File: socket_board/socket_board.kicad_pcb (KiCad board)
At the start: 2 copper layers, 90.2 x 35.6 mm, 8 parts, among them J1 Barrel_Jack_Switch, J2 DIN-5_180degree, J3 DIN-5_180degree, J4 AudioJack3, J5 AudioJack3, J6 Conn_01x02_Male, J7 Conn_01x04_Male, J8 Conn_01x05_Male

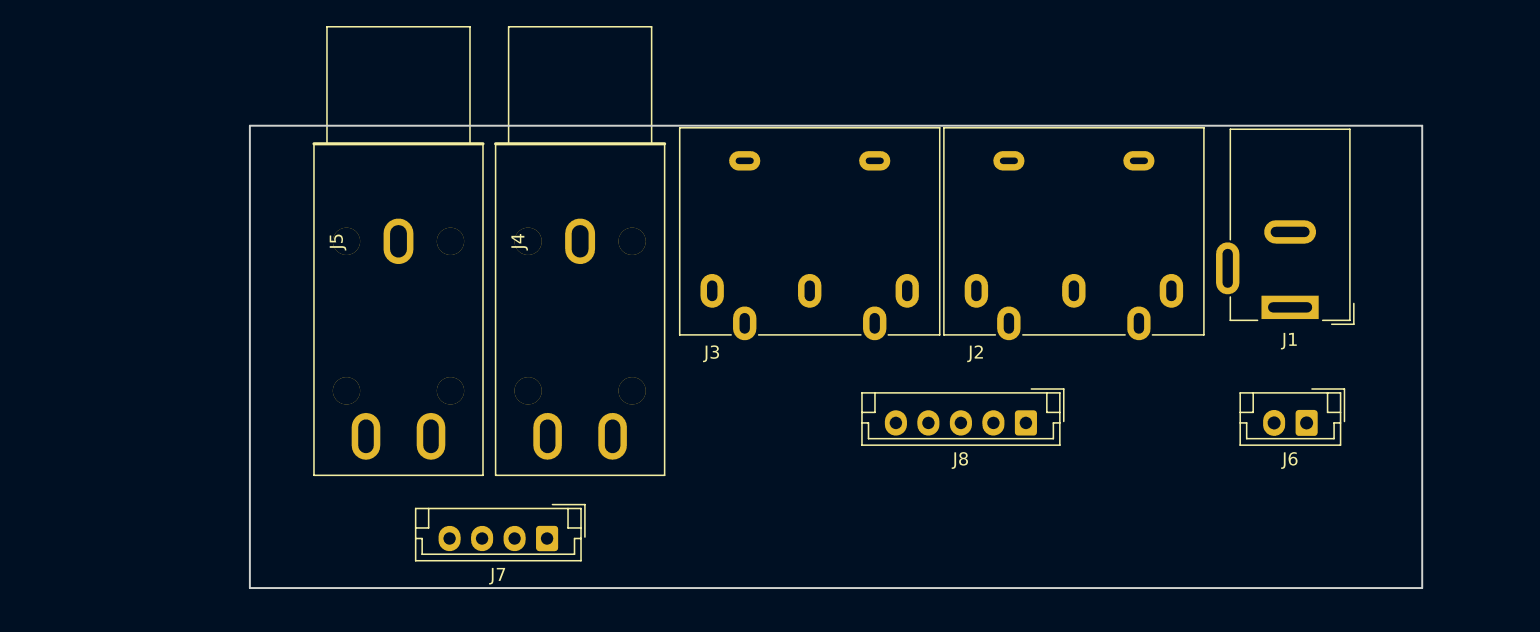
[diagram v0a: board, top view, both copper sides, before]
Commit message: Adjusting socket board dimensions.
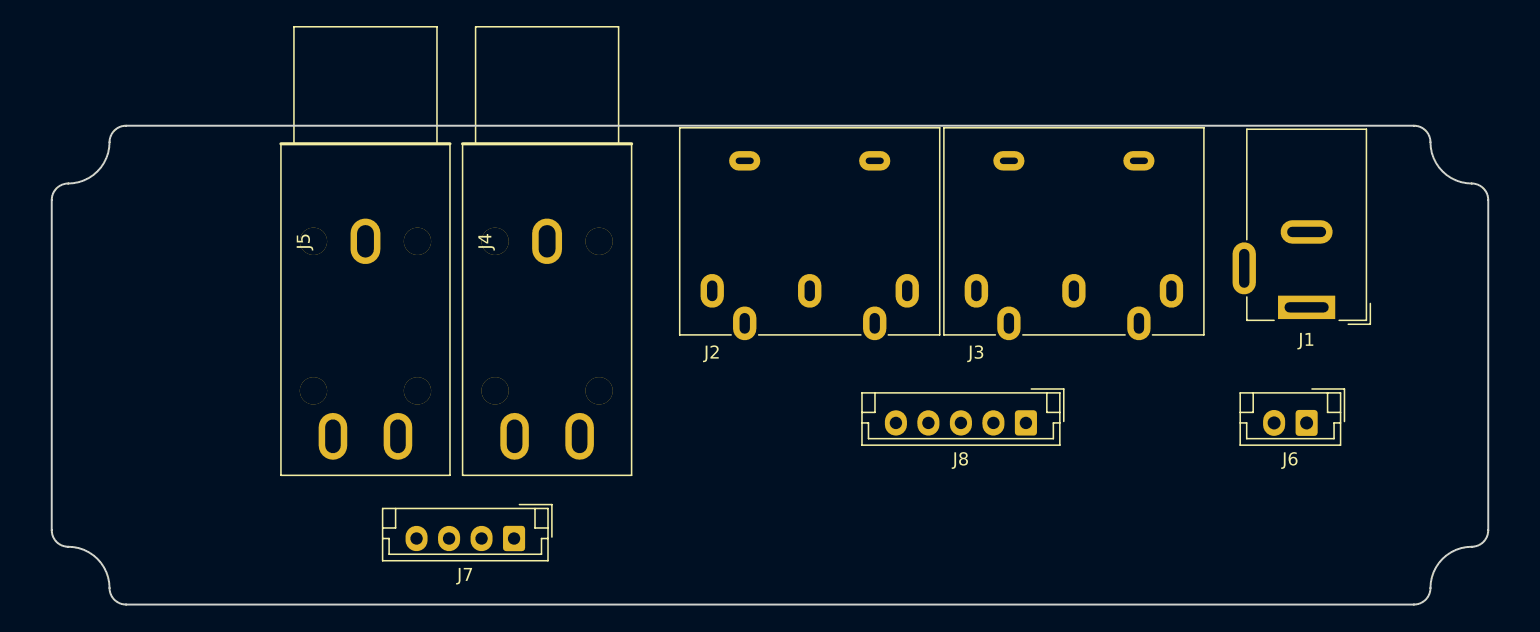
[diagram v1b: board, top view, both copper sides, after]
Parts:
- moved J2 20.3 mm to (139.7, 99.1)
- moved J3 20.3 mm to (160.0, 99.1)
- moved J7 2.54 mm to (124.5, 118.1)
- moved J4 2.54 mm to (127.0, 95.2)
- moved J5 2.54 mm to (113.0, 95.2)
- moved J1 1.27 mm to (185.4, 100.3)
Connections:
- J8 pad 1: MIN_5 -> MOUT_5
- J8 pad 2: MIN_4 -> MOUT_2
- J8 pad 3: MOUT_5 -> MOUT_4
- J8 pad 4: MOUT_2 -> MIN_5
- J8 pad 5: MOUT_4 -> MIN_4
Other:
- board size 90.2 x 35.6 mm -> 110.5 x 36.8 mm
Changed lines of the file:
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@@
   (general
     (thickness 1.6)
-    (drawings 4)
+    (drawings 23)
     (tracks 0)
     (zones 0)
@@
     (zone_45_only no)
     (trace_min 0.2)
-    (segment_width 0.2)
+    (segment_width 0.15)
     (edge_width 0.15)
     (via_size 0.8)
@@
   )
   (module Connector_BarrelJack:BarrelJack_Wuerth_6941xx301002 (layer F.Cu)
-    (at 184.15 100.33 180)
+    (at 185.42 100.33 180)
     (descr "Wuerth electronics barrel jack connector (5.5mm outher diameter, inner diameter 2.05mm or 2.55mm depending on exact order number), See: http://katalog.we-online.de/em/datasheet/6941xx301002.pdf")
     (tags "connector barrel jack")
@@
   )
   (module Connectors:DIN5MIDI-OOTDTY (layer F.Cu)
-    (at 160.02 99.06)
+    (at 139.7 99.06)
     (descr "standard DIN connector, 5 pins, midi")
     (tags "OOTDTY DIN 5-pins connector midi")
@@
   )
   (module Connectors:DIN5MIDI-OOTDTY (layer F.Cu)
-    (at 139.7 99.06)
+    (at 160.02 99.06)
     (descr "standard DIN connector, 5 pins, midi")
     (tags "OOTDTY DIN 5-pins connector midi")
@@
   )
   (module Connectors:phone-jack-6.3 (layer F.Cu)
-    (at 129.54 95.25 270)
+    (at 127 95.25 270)
     (descr "Phone Jack 6.3 mm")
     (tags "jack connector")
@@
   )
   (module Connectors:phone-jack-6.3 (layer F.Cu)
-    (at 115.57 95.25 270)
+    (at 113.03 95.25 270)
     (descr "Phone Jack 6.3 mm")
     (tags "jack connector")
@@
   )
   (module Connector_JST:JST_EH_B04B-EH-A_1x04_P2.50mm_Vertical (layer F.Cu)
-    (at 127 118.11 180)
+    (at 124.46 118.11 180)
     (descr "JST EH series connector, B04B-EH-A (http://www.jst-mfg.com/product/pdf/eng/eEH.pdf), generated with kicad-footprint-generator")
     (tags "connector JST EH side entry")
@@
     )
     (pad 1 thru_hole roundrect (at 0 0 180) (size 1.7 1.95) (drill 0.95) (layers *.Cu *.Mask) (roundrect_rratio 0.147059)
+      (net 9 MOUT_5))
+    (pad 2 thru_hole oval (at 2.5 0 180) (size 1.7 1.95) (drill 0.95) (layers *.Cu *.Mask)
+      (net 11 MOUT_2))
+    (pad 3 thru_hole oval (at 5 0 180) (size 1.7 1.95) (drill 0.95) (layers *.Cu *.Mask)
+      (net 13 MOUT_4))
+    (pad 4 thru_hole oval (at 7.5 0 180) (size 1.7 1.95) (drill 0.95) (layers *.Cu *.Mask)
       (net 8 MIN_5))
-    (pad 2 thru_hole oval (at 2.5 0 180) (size 1.7 1.95) (drill 0.95) (layers *.Cu *.Mask)
+    (pad 5 thru_hole oval (at 10 0 180) (size 1.7 1.95) (drill 0.95) (layers *.Cu *.Mask)
       (net 4 MIN_4))
-    (pad 3 thru_hole oval (at 5 0 180) (size 1.7 1.95) (drill 0.95) (layers *.Cu *.Mask)
-      (net 9 MOUT_5))
-    (pad 4 thru_hole oval (at 7.5 0 180) (size 1.7 1.95) (drill 0.95) (layers *.Cu *.Mask)
-      (net 11 MOUT_2))
-    (pad 5 thru_hole oval (at 10 0 180) (size 1.7 1.95) (drill 0.95) (layers *.Cu *.Mask)
-      (net 13 MOUT_4))
     (model ${KISYS3DMOD}/Connector_JST.3dshapes/JST_EH_B05B-EH-A_1x05_P2.50mm_Vertical.wrl
       (at (xyz 0 0 0))
@@
     )
   )
-  (gr_line (start 104.14 121.92) (end 104.14 86.36) (layer Edge.Cuts) (width 0.15))
-  (gr_line (start 194.31 121.92) (end 104.14 121.92) (layer Edge.Cuts) (width 0.15))
-  (gr_line (start 194.31 86.36) (end 194.31 121.92) (layer Edge.Cuts) (width 0.15))
-  (gr_line (start 104.14 86.36) (end 194.31 86.36) (layer Edge.Cuts) (width 0.15))
+  (gr_line (start 199.39 92.075) (end 199.39 117.475) (layer Edge.Cuts) (width 0.15))
+  (gr_line (start 88.9 117.475) (end 88.9 92.075) (layer Edge.Cuts) (width 0.15))
+  (gr_arc (start 198.12 121.92) (end 194.945 121.92) (angle 90) (layer Edge.Cuts) (width 0.15))
+  (gr_arc (start 90.17 121.92) (end 90.17 118.745) (angle 90) (layer Edge.Cuts) (width 0.15))
+  (gr_arc (start 90.17 87.63) (end 93.345 87.63) (angle 90) (layer Edge.Cuts) (width 0.15))
+  (gr_arc (start 94.615 121.92) (end 94.615 123.19) (angle 90) (layer Edge.Cuts) (width 0.15))
+  (gr_arc (start 90.17 117.475) (end 90.17 118.745) (angle 90) (layer Edge.Cuts) (width 0.15))
+  (gr_arc (start 198.12 117.475) (end 199.39 117.475) (angle 90) (layer Edge.Cuts) (width 0.15))
+  (gr_arc (start 193.675 121.92) (end 194.945 121.92) (angle 90) (layer Edge.Cuts) (width 0.15))
+  (gr_arc (start 90.17 92.075) (end 88.9 92.075) (angle 90) (layer Edge.Cuts) (width 0.15))
+  (gr_arc (start 94.615 87.63) (end 93.345 87.63) (angle 90) (layer Edge.Cuts) (width 0.15))
+  (gr_arc (start 198.12 92.075) (end 198.12 90.805) (angle 90) (layer Edge.Cuts) (width 0.15))
+  (gr_line (start 179.07 87.63) (end 179.07 102.87) (layer F.Fab) (width 0.15))
+  (gr_line (start 135.89 87.63) (end 135.89 102.87) (layer F.Fab) (width 0.15))
+  (gr_line (start 137.16 104.14) (end 177.8 104.14) (layer F.Fab) (width 0.15))
+  (gr_arc (start 177.8 102.87) (end 179.07 102.87) (angle 90) (layer F.Fab) (width 0.15))
+  (gr_arc (start 137.16 102.87) (end 137.16 104.14) (angle 90) (layer F.Fab) (width 0.15))
+  (gr_arc (start 180.34 87.63) (end 179.07 87.63) (angle 90) (layer F.Fab) (width 0.15))
+  (gr_arc (start 134.62 87.63) (end 134.62 86.36) (angle 90) (layer F.Fab) (width 0.15))
+  (gr_arc (start 198.12 87.63) (end 198.12 90.805) (angle 90) (layer Edge.Cuts) (width 0.15))
+  (gr_arc (start 193.675 87.63) (end 193.675 86.36) (angle 90) (layer Edge.Cuts) (width 0.15))
+  (gr_line (start 193.675 123.19) (end 94.615 123.19) (layer Edge.Cuts) (width 0.15))
+  (gr_line (start 94.615 86.36) (end 193.675 86.36) (layer Edge.Cuts) (width 0.15))
 )

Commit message: Printed and tested layout version.
USB still on upper board.
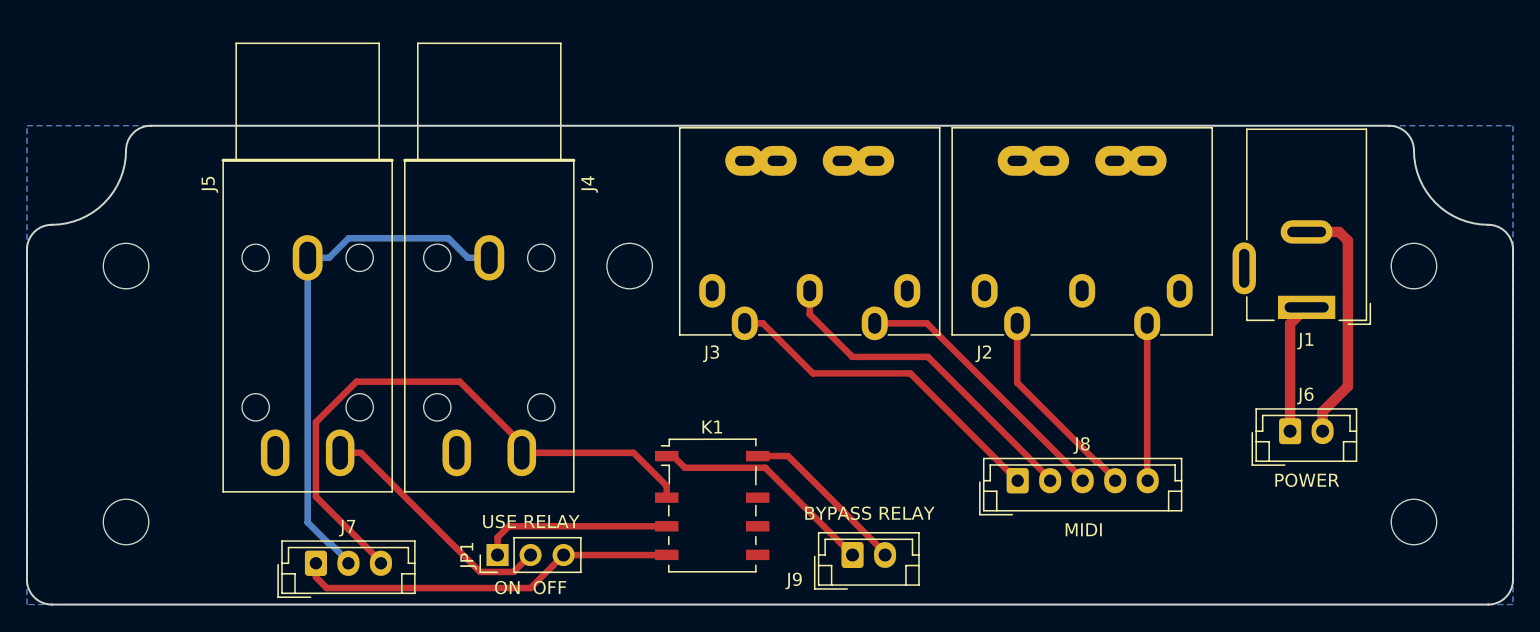
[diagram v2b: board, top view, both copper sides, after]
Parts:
- added J9: Conn_01x02_Male, Connector_JST:JST_EH_B02B-EH-A_1x02_P2.50mm_Vertical, F.Cu at (150.5, 119.4)
- added JP1: Jumper_3_Bridged12, Connector_PinHeader_2.54mm:PinHeader_1x03_P2.54mm_Vertical, F.Cu at (123.2, 119.4)
- added K1: G6K-2, Relay_SMD:Relay_DPDT_Omron_G6K-2F-Y, F.Cu at (139.7, 115.6)
- added REF**: MountingHole_3.5mm, MountingHole:MountingHole_3.5mm, F.Cu at (133.3, 97.2)
- added REF**: MountingHole_3.5mm, MountingHole:MountingHole_3.5mm, F.Cu at (94.6, 116.8)
- added REF**: MountingHole_3.5mm, MountingHole:MountingHole_3.5mm, F.Cu at (193.7, 116.8)
- added REF**: MountingHole_3.5mm, MountingHole:MountingHole_3.5mm, F.Cu at (193.7, 97.2)
- added REF**: MountingHole_3.5mm, MountingHole:MountingHole_3.5mm, F.Cu at (94.6, 97.2)
- added REF**: KiCad-Logo2_5mm_SilkScreen, Symbol:KiCad-Logo2_5mm_SilkScreen, B.Cu at (142.9, 109.2)
- J7: value Conn_01x04_Male -> Conn_01x03_Male; footprint Connector_JST:JST_EH_B04B-EH-A_1x04_P2.50mm_Vertical -> Connector_JST:JST_EH_B03B-EH-A_1x03_P2.50mm_Vertical
- moved J2 21.0 mm to (160.7, 99.1)
- moved J3 20.3 mm to (139.7, 99.1)
- moved J7 15.4 mm to (109.2, 120.0), turned to 0 degrees
- moved J5 4.62 mm to (108.6, 96.5)
- moved J4 4.62 mm to (122.6, 96.5)
- moved J8 4.49 mm to (163.2, 113.7), turned to 0 degrees
- moved J6 1.42 mm to (184.2, 109.9), turned to 0 degrees
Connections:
- J4 pad S: IN_S -> GND
- J5 pad S: OUT_S -> GND
- J5 pad T: OUT_T -> Net-(J5-PadT)
- J7 pad 1: IN_S -> OUT_T
- J7 pad 2: IN_T -> GND
- J7 pad 3: OUT_S -> IN_T
- J8 pad 1: MOUT_5 -> MOUT_4
- J8 pad 3: MOUT_4 -> MOUT_5
- J8 pad 4: MIN_5 -> MIN_4
- J8 pad 5: MIN_4 -> MIN_5
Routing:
- net IN_T: track 0.00 -> 45.8 mm
- net GND: track 0.00 -> 40.1 mm
- net OUT_T: track 0.00 -> 29.5 mm
- net MOUT_4: track 0.00 -> 26.0 mm
- net MOUT_2: track 0.00 -> 25.7 mm
- net MOUT_5: track 0.00 -> 21.1 mm
- net Net-(J5-PadT): track 0.00 -> 19.0 mm
- net POW2: track 0.00 -> 18.9 mm
- net REL+: track 0.00 -> 17.4 mm
- net MIN_4: track 0.00 -> 15.3 mm
- net Net-(JP1-Pad1): track 0.00 -> 14.7 mm
- net REL-: track 0.00 -> 13.0 mm
- net MIN_5: track 0.00 -> 12.1 mm
- net POW1: track 0.00 -> 10.1 mm
- added copper zone on B.Cu, net GND
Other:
- board size 110.5 x 36.8 mm -> 114.3 x 36.8 mm
- net class Default: trace_width 0.25 -> 0.5
- board text added: "2011.11.12"
- board text added: "BYPASS RELAY"
- board text added: "MIDI"
- board text added: "ON OFF"
- board text added: "POWER"
- board text added: "USE RELAY"
- board text added: "https://github.com/mar0x/pq-4"
- board text added: "socket_board"

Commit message: Production version 2019.11.19.
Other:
- board text added: "+"
- board text added: "-"
- board text added: "2011.11.18"
- board text added: "github.com/mar0x/pq-4"
- board text removed: "2011.11.12"
- board text removed: "https://github.com/mar0x/pq-4"
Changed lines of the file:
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@@
   (general
     (thickness 1.6)
-    (drawings 34)
+    (drawings 36)
     (tracks 68)
     (zones 0)
@@
       (outputformat 1)
       (mirror false)
-      (drillshape 1)
+      (drillshape 0)
       (scaleselection 1)
-      (outputdirectory ""))
+      (outputdirectory "gerber/"))
   )
   (net 0 "")
@@
     (descr "JST EH series connector, B02B-EH-A (http://www.jst-mfg.com/product/pdf/eng/eEH.pdf), generated with kicad-footprint-generator")
     (tags "connector JST EH side entry")
-    (fp_text reference J6 (at 1.25 -2.8) (layer F.SilkS)
-      (effects (font (size 1 1) (thickness 0.15)))
-    )
-    (fp_text value Conn_01x02_Male (at 1.25 3.4) (layer F.Fab)
+    (fp_text reference J6 (at 6.35 1.905) (layer F.SilkS)
+      (effects (font (size 1 1) (thickness 0.15)))
+    )
+    (fp_text value Conn_01x02_Male (at 1.25 3.4) (layer F.Fab) hide
       (effects (font (size 1 1) (thickness 0.15)))
     )
@@
     (descr "JST EH series connector, B05B-EH-A (http://www.jst-mfg.com/product/pdf/eng/eEH.pdf), generated with kicad-footprint-generator")
     (tags "connector JST EH side entry")
-    (fp_text reference J8 (at 5 -2.8) (layer F.SilkS)
-      (effects (font (size 1 1) (thickness 0.15)))
-    )
-    (fp_text value Conn_01x05_Male (at 5 3.4) (layer F.Fab)
+    (fp_text reference J8 (at 13.97 1.905) (layer F.SilkS)
+      (effects (font (size 1 1) (thickness 0.15)))
+    )
+    (fp_text value Conn_01x05_Male (at 5 3.4) (layer F.Fab) hide
       (effects (font (size 1 1) (thickness 0.15)))
     )
@@
       (effects (font (size 1 1) (thickness 0.15)))
     )
-    (fp_text value Conn_01x02_Male (at 1.25 3.4) (layer F.Fab)
+    (fp_text value Conn_01x02_Male (at 1.25 3.4) (layer F.Fab) hide
       (effects (font (size 1 1) (thickness 0.15)))
     )
@@
       (effects (font (size 1 1) (thickness 0.15)))
     )
-    (fp_text value Jumper_3_Bridged12 (at 0 7.41 90) (layer F.Fab)
+    (fp_text value Jumper_3_Bridged12 (at 0 7.41 90) (layer F.Fab) hide
       (effects (font (size 1 1) (thickness 0.15)))
     )
@@
     (descr "JST EH series connector, B03B-EH-A (http://www.jst-mfg.com/product/pdf/eng/eEH.pdf), generated with kicad-footprint-generator")
     (tags "connector JST EH side entry")
-    (fp_text reference J7 (at 2.5 -2.8) (layer F.SilkS)
-      (effects (font (size 1 1) (thickness 0.15)))
-    )
-    (fp_text value Conn_01x03_Male (at 2.5 3.4) (layer F.Fab)
+    (fp_text reference J7 (at 8.89 1.27) (layer F.SilkS)
+      (effects (font (size 1 1) (thickness 0.15)))
+    )
+    (fp_text value Conn_01x03_Male (at 2.5 3.4) (layer F.Fab) hide
       (effects (font (size 1 1) (thickness 0.15)))
     )
@@
       (xy -2.9464 2.607733) (xy -2.9464 2.510946)) (layer B.SilkS) (width 0.01))
   )
+  (gr_text + (at 146.685 118.745) (layer F.SilkS)
+    (effects (font (size 1 1.1) (thickness 0.2)))
+  )
+  (gr_text - (at 156.845 118.745) (layer F.SilkS)
+    (effects (font (size 1 1.1) (thickness 0.2)))
+  )
   (gr_text "ON  OFF" (at 125.73 121.92) (layer F.SilkS)
-    (effects (font (size 1 1) (thickness 0.2)))
+    (effects (font (size 1 1.1) (thickness 0.2)))
   )
   (gr_text "USE RELAY" (at 125.73 116.84) (layer F.SilkS)
-    (effects (font (size 1 1) (thickness 0.2)))
+    (effects (font (size 1 1.1) (thickness 0.2)))
   )
   (gr_text POWER (at 185.42 113.665) (layer F.SilkS)
-    (effects (font (size 1 1) (thickness 0.2)))
-  )
-  (gr_text "BYPASS RELAY" (at 151.765 116.205) (layer F.SilkS)
-    (effects (font (size 1 1) (thickness 0.2)))
+    (effects (font (size 1 1.1) (thickness 0.2)))
+  )
+  (gr_text "BYPASS RELAY" (at 151.765 115.57) (layer F.SilkS)
+    (effects (font (size 1 1.1) (thickness 0.2)))
   )
   (gr_text MIDI (at 168.275 117.475) (layer F.SilkS)
-    (effects (font (size 1 1) (thickness 0.2)))
-  )
-  (gr_text https://github.com/mar0x/pq-4 (at 114.935 88.9) (layer B.SilkS)
-    (effects (font (size 0.8 0.7) (thickness 0.15)) (justify mirror))
-  )
-  (gr_text 2011.11.12 (at 105.41 103.505) (layer B.SilkS)
-    (effects (font (size 0.8 0.8) (thickness 0.2)) (justify mirror))
+    (effects (font (size 1 1.1) (thickness 0.2)))
+  )
+  (gr_text github.com/mar0x/pq-4 (at 114.935 88.9) (layer B.SilkS)
+    (effects (font (size 0.9 1) (thickness 0.15)) (justify mirror))
+  )
+  (gr_text 2011.11.18 (at 105.41 103.505) (layer B.SilkS)
+    (effects (font (size 0.9 0.9) (thickness 0.2)) (justify mirror))
   )
   (gr_text socket_board (at 115.57 101.6) (layer B.SilkS)
